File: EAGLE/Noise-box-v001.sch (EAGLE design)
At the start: 40 parts, among them J1 AVR_SPI_PROG_3X22X3_LOCK, J2 BATT, J4 MICRO-SD_CARD_SOCKET, J5 AUDIO_JACK_3.5MM_SMD, U1 ATMEGA328P_TQFP, U2 MIC5219 3.3V, U3 MCP73831, Y1 12.288MHz

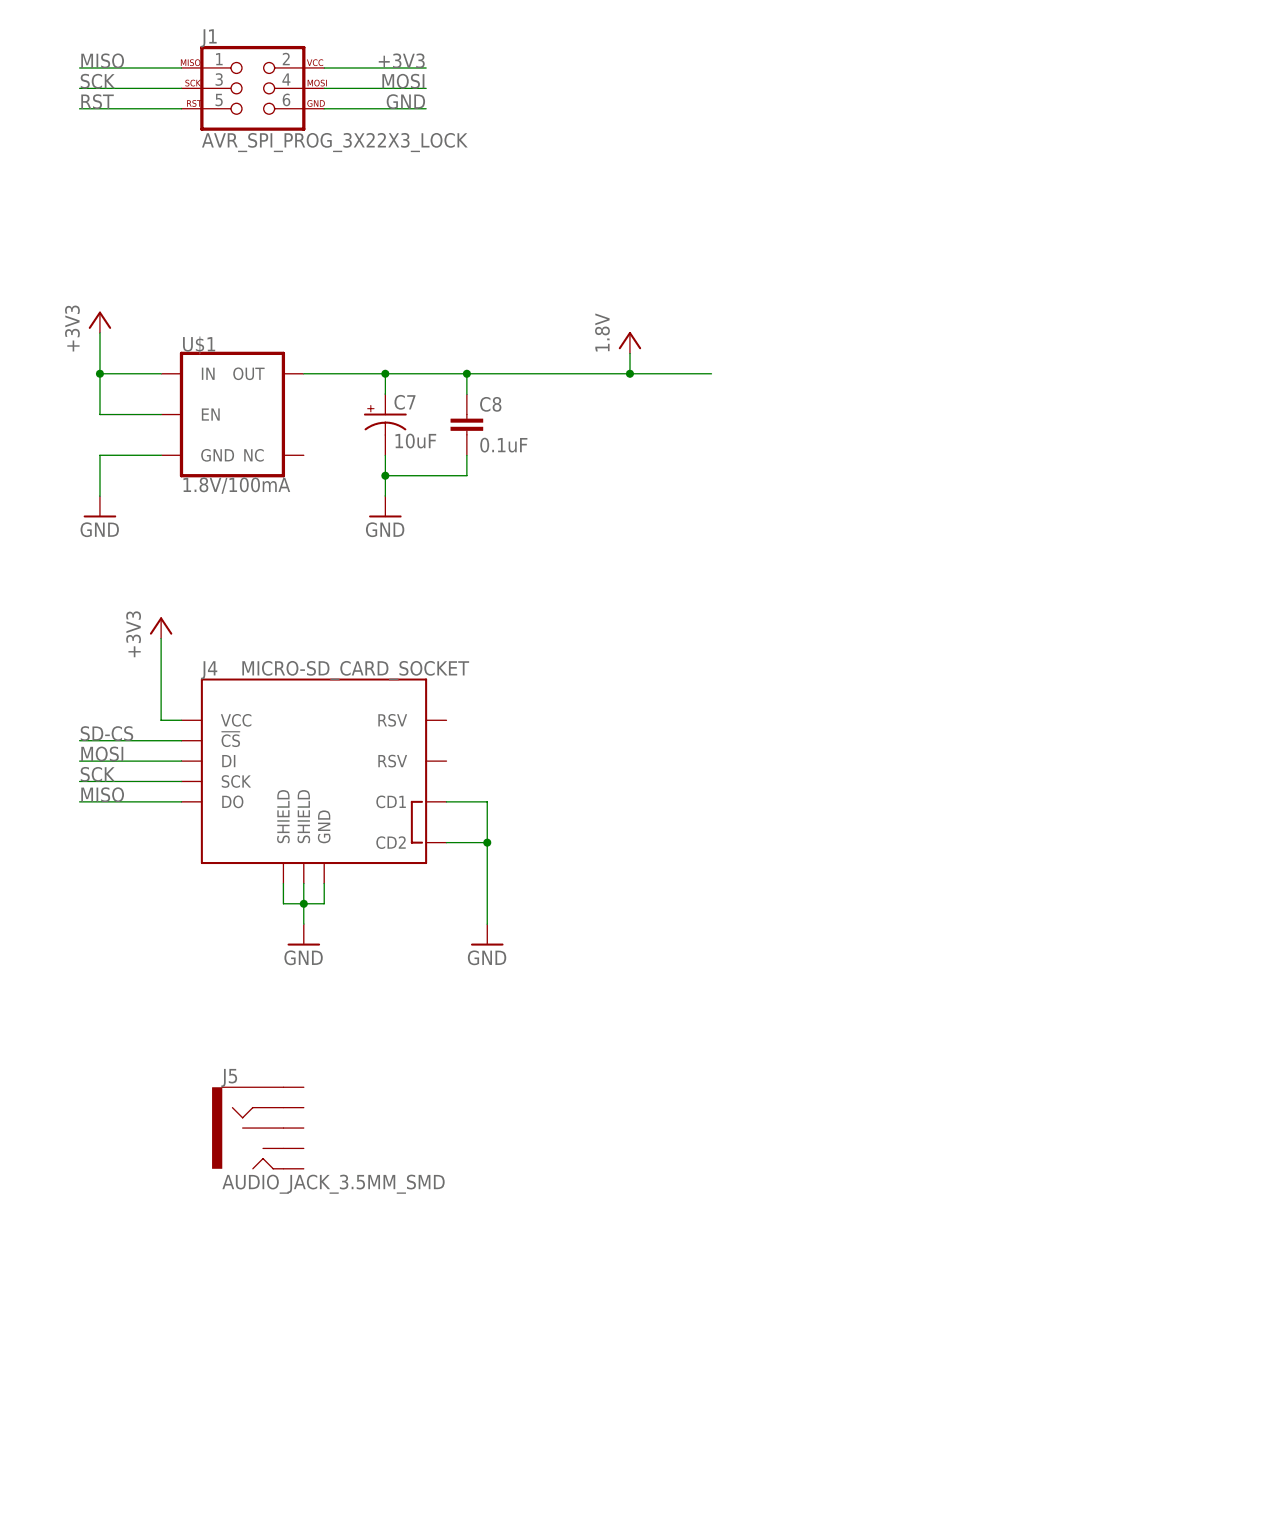
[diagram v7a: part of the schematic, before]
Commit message: Audio amp
Added simple audio amplifier
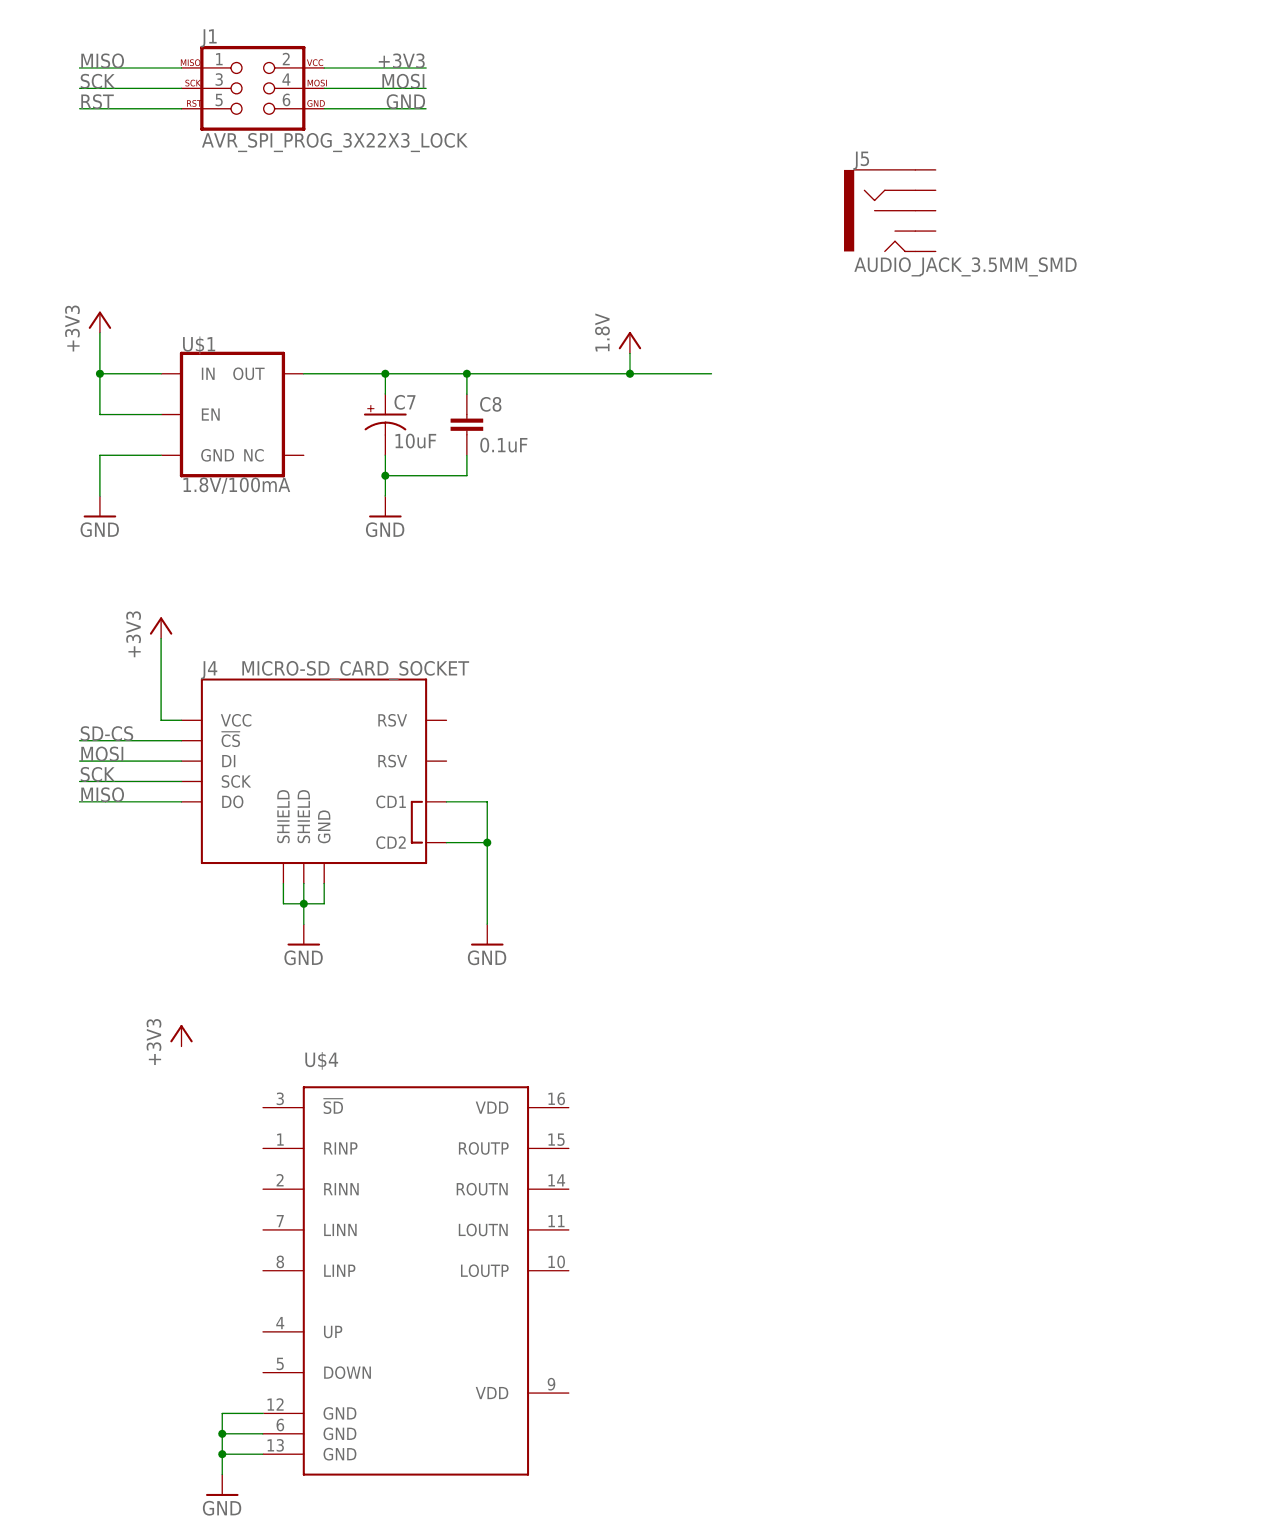
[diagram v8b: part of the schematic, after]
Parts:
- added U$4: (no value), RJC:PAM8407
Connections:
- net GND: now also U$4.GND@1, U$4.GND@2, U$4.GND@3
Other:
- moved on the sheet: J5
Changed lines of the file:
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@@
 <part name="GND21" library="supply1" deviceset="GND" device=""/>
 <part name="P+4" library="supply1" deviceset="VCC" device="" value="1.8V"/>
+<part name="U$4" library="RJC" deviceset="PAM8407" device=""/>
+<part name="+3V12" library="supply1" deviceset="+3V3" device=""/>
+<part name="GND22" library="supply1" deviceset="GND" device=""/>
 </parts>
 <sheets>
@@
 <instance part="GND12" gate="1" x="60.96" y="73.66"/>
 <instance part="U$2" gate="G$1" x="228.6" y="71.12"/>
-<instance part="J5" gate="G$1" x="33.02" y="50.8"/>
+<instance part="J5" gate="G$1" x="111.76" y="165.1"/>
 <instance part="U$3" gate="G$1" x="347.98" y="226.06"/>
 <instance part="Y1" gate="G$1" x="281.94" y="223.52" smashed="yes" rot="R90">
@@
 <instance part="GND21" gate="1" x="421.64" y="254"/>
 <instance part="P+4" gate="VCC" x="421.64" y="271.78"/>
+<instance part="U$4" gate="G$1" x="50.8" y="35.56"/>
+<instance part="+3V12" gate="G$1" x="22.86" y="63.5"/>
+<instance part="GND22" gate="1" x="27.94" y="5.08"/>
 </instances>
 <busses>
@@
 <wire x1="421.64" y1="256.54" x2="421.64" y2="259.08" width="0.1524" layer="91"/>
 </segment>
+<segment>
+<pinref part="U$4" gate="G$1" pin="GND@3"/>
+<pinref part="GND22" gate="1" pin="GND"/>
+<wire x1="33.02" y1="10.16" x2="27.94" y2="10.16" width="0.1524" layer="91"/>
+<wire x1="27.94" y1="10.16" x2="27.94" y2="7.62" width="0.1524" layer="91"/>
+<pinref part="U$4" gate="G$1" pin="GND@1"/>
+<wire x1="33.02" y1="12.7" x2="27.94" y2="12.7" width="0.1524" layer="91"/>
+<wire x1="27.94" y1="12.7" x2="27.94" y2="10.16" width="0.1524" layer="91"/>
+<junction x="27.94" y="10.16"/>
+<pinref part="U$4" gate="G$1" pin="GND@2"/>
+<wire x1="33.02" y1="15.24" x2="27.94" y2="15.24" width="0.1524" layer="91"/>
+<wire x1="27.94" y1="15.24" x2="27.94" y2="12.7" width="0.1524" layer="91"/>
+<junction x="27.94" y="12.7"/>
+</segment>
 </net>
